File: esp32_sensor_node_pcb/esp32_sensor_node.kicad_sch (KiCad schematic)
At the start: 21 parts, among them J1 Conn_02x10_Top_Bottom, Q1 2N7002K, SW1 SW_DIP_x01, SW2 SW_DIP_x01, U1 HT7833, U2 ESP32-WROOM-E, U3 MAX3483AEASA+

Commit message: Updated schematic
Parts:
- added C6: 22uF, Capacitor_SMD:C_0603_1608Metric, symbol Device:C_Small
- R2: value 500R -> 1.91K
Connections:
- net GND: now also C6.2
- net 3V3 renamed +3.3V
- net +3.3V: now also JST_XH_SOIL5V1.1 (Pin_1), U3.8 (VCC), C6.1
- net 5V renamed +5V
- net +5V: no longer JST_XH_SOIL5V1.1 (Pin_1), U3.8 (VCC)

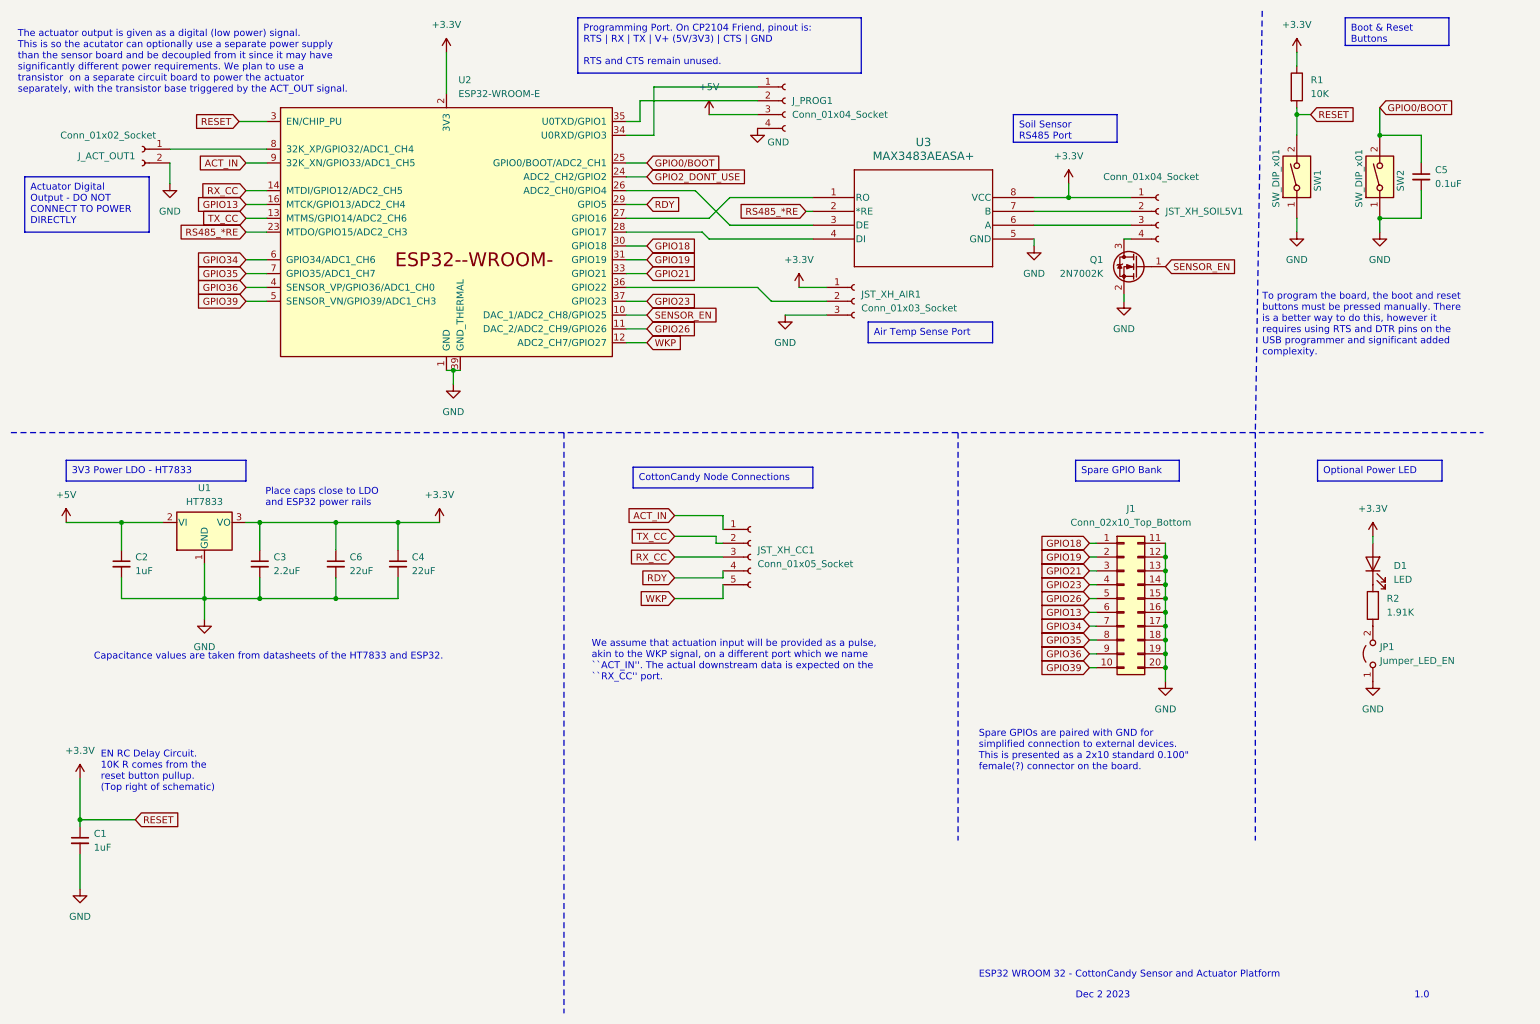
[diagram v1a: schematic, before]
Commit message: Added big 0805 22u capacitor, fixed reset capacitor, add capacitor for max ic decoupling
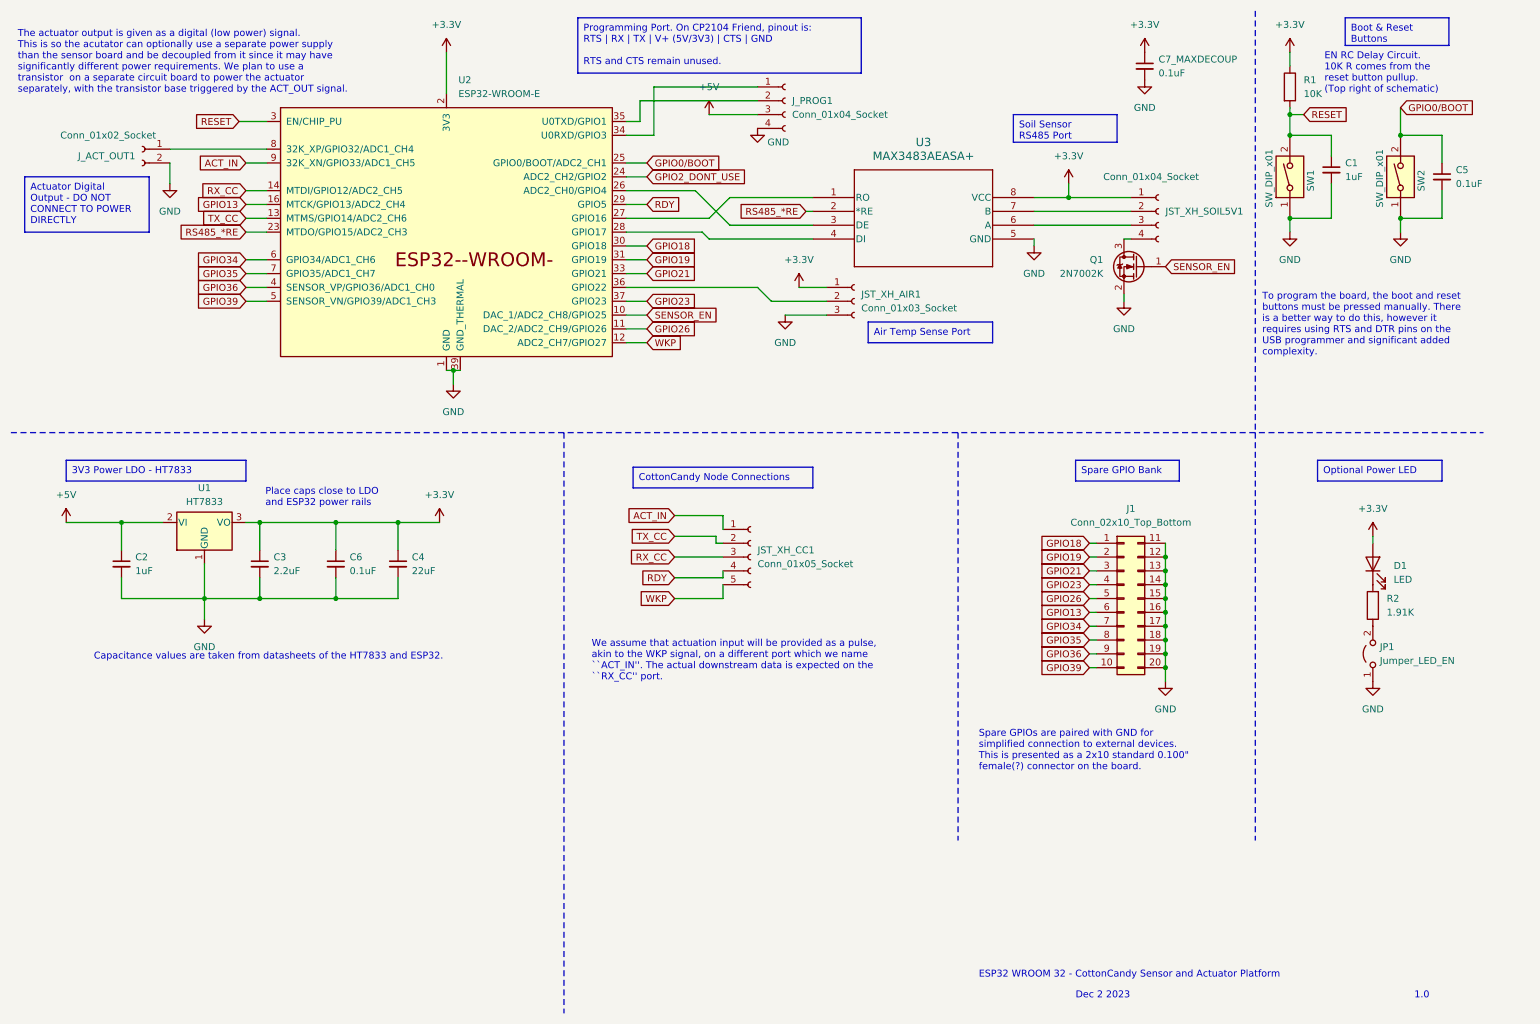
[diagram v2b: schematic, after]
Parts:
- added C7_MAXDECOUP: 0.1uF, Capacitor_SMD:C_0603_1608Metric, symbol Device:C_Small
- C4: footprint Capacitor_SMD:C_0603_1608Metric -> Capacitor_SMD:C_0805_2012Metric
- C6: value 22uF -> 0.1uF
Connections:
- net +3.3V: now also C7_MAXDECOUP.1; no longer C1.1, R1.2, SW1.2, U2.3 (EN/CHIP_PU)
- net GND: now also C7_MAXDECOUP.2
- new net RESET: C1.1, R1.2, SW1.2, U2.3 (EN/CHIP_PU)
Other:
- moved on the sheet: C5, R1, SW1, SW2

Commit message: Add mounting holes
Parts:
- added H1, H2, H3, H4: MountingHole_Pad, MountingHole:MountingHole_3.2mm_M3, symbol Mechanical:MountingHole_Pad
- renumbered C2 to C1, C3 to C2, C6 to C3, C1 to C5, C5 to C6, C7_MAXDECOUP to C7_MAXDECOUP1

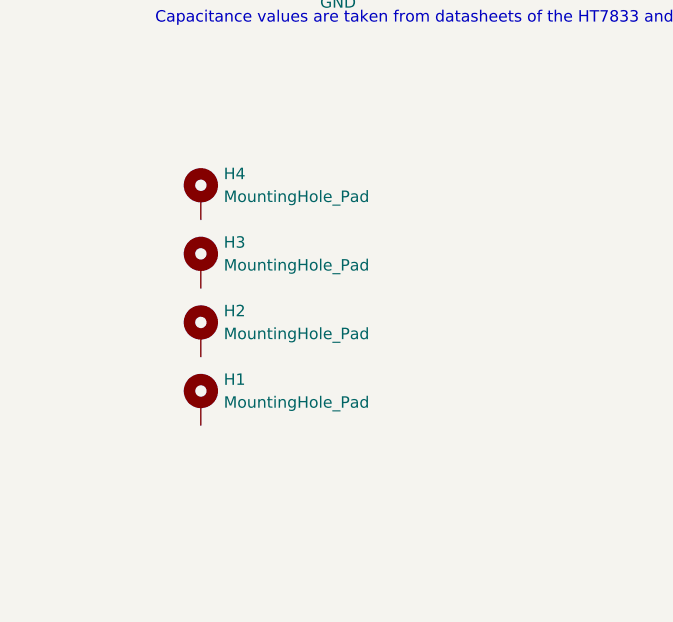
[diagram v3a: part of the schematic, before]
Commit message: Setup initial board layout
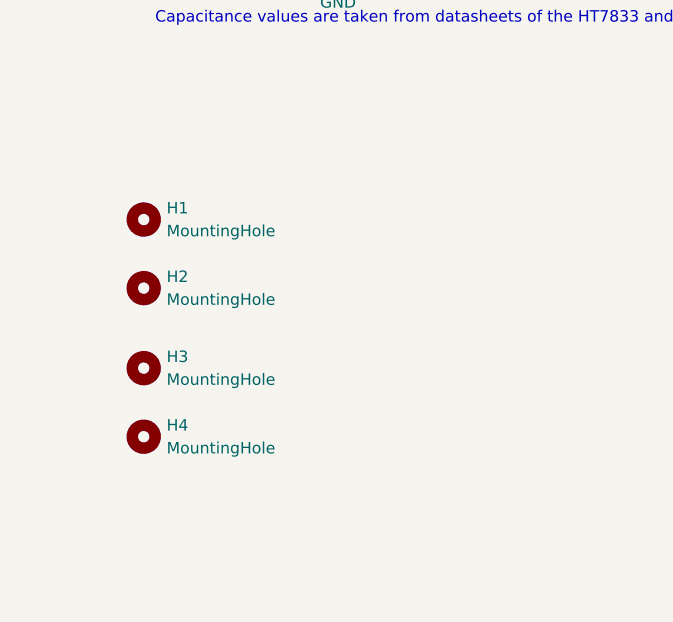
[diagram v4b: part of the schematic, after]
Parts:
- removed H1, H2, H3, H4: MountingHole_Pad, MountingHole:MountingHole_3.2mm_M3, symbol Mechanical:MountingHole_Pad
- added H1, H2, H3, H4: MountingHole, MountingHole:MountingHole_3.2mm_M3, symbol Mechanical:MountingHole
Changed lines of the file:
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@@
-    )
-  )
-  (symbol (lib_id "Mechanical:MountingHole_Pad") (at 33.02 173.99 0) (unit 1)
-    (in_bom yes) (on_board yes) (dnp no) (fields_autoplaced)
-    (property "Reference" "H1" (at 35.56 171.45 0)
-      (effects (font (size 1.27 1.27)) (justify left))
-    )
-    (property "Value" "MountingHole_Pad" (at 35.56 173.99 0)
-      (effects (font (size 1.27 1.27)) (justify left))
-    )
-    (property "Footprint" "MountingHole:MountingHole_3.2mm_M3" (at 33.02 173.99 0)
-      (effects (font (size 1.27 1.27)) hide)
-    )
-    (property "Datasheet" "~" (at 33.02 173.99 0)
-      (effects (font (size 1.27 1.27)) hide)
-    )
-    (pin "1")
-    (instances
-      (project "esp32_sensor_node"
-        (path "/f305b47d-1a34-49f4-94a4-22a58fb9ed31"
-          (reference "H1") (unit 1)
-        )
-      )
     )
   )
@@
     )
   )
-  (symbol (lib_id "Mechanical:MountingHole_Pad") (at 33.02 166.37 0) (unit 1)
-    (in_bom yes) (on_board yes) (dnp no) (fields_autoplaced)
-    (property "Reference" "H2" (at 35.56 163.83 0)
-      (effects (font (size 1.27 1.27)) (justify left))
-    )
-    (property "Value" "MountingHole_Pad" (at 35.56 166.37 0)
-      (effects (font (size 1.27 1.27)) (justify left))
-    )
-    (property "Footprint" "MountingHole:MountingHole_3.2mm_M3" (at 33.02 166.37 0)
-      (effects (font (size 1.27 1.27)) hide)
-    )
-    (property "Datasheet" "~" (at 33.02 166.37 0)
-      (effects (font (size 1.27 1.27)) hide)
-    )
-    (pin "1")
-    (instances
-      (project "esp32_sensor_node"
-        (path "/f305b47d-1a34-49f4-94a4-22a58fb9ed31"
-          (reference "H2") (unit 1)
-        )
-      )
-    )
-  )
   (symbol (lib_id "power:GND") (at 247.65 53.34 0) (unit 1)
     (in_bom yes) (on_board yes) (dnp no) (fields_autoplaced)
@@
         (path "/f305b47d-1a34-49f4-94a4-22a58fb9ed31"
           (reference "JP1") (unit 1)
-        )
-      )
-    )
-  )
-  (symbol (lib_id "Mechanical:MountingHole_Pad") (at 33.02 158.75 0) (unit 1)
-    (in_bom yes) (on_board yes) (dnp no) (fields_autoplaced)
-    (property "Reference" "H3" (at 35.56 156.21 0)
-      (effects (font (size 1.27 1.27)) (justify left))
-    )
-    (property "Value" "MountingHole_Pad" (at 35.56 158.75 0)
-      (effects (font (size 1.27 1.27)) (justify left))
-    )
-    (property "Footprint" "MountingHole:MountingHole_3.2mm_M3" (at 33.02 158.75 0)
-      (effects (font (size 1.27 1.27)) hide)
-    )
-    (property "Datasheet" "~" (at 33.02 158.75 0)
-      (effects (font (size 1.27 1.27)) hide)
-    )
-    (pin "1")
-    (instances
-      (project "esp32_sensor_node"
-        (path "/f305b47d-1a34-49f4-94a4-22a58fb9ed31"
-          (reference "H3") (unit 1)
         )
       )
@@
     )
   )
+  (symbol (lib_id "Mechanical:MountingHole") (at 26.67 170.18 0) (unit 1)
+    (in_bom yes) (on_board yes) (dnp no) (fields_autoplaced)
+    (property "Reference" "H3" (at 29.21 168.91 0)
+      (effects (font (size 1.27 1.27)) (justify left))
+    )
+    (property "Value" "MountingHole" (at 29.21 171.45 0)
+      (effects (font (size 1.27 1.27)) (justify left))
+    )
+    (property "Footprint" "MountingHole:MountingHole_3.2mm_M3" (at 26.67 170.18 0)
+      (effects (font (size 1.27 1.27)) hide)
+    )
+    (property "Datasheet" "~" (at 26.67 170.18 0)
+      (effects (font (size 1.27 1.27)) hide)
+    )
+    (instances
+      (project "esp32_sensor_node"
+        (path "/f305b47d-1a34-49f4-94a4-22a58fb9ed31"
+          (reference "H3") (unit 1)
+        )
+      )
+    )
+  )
   (symbol (lib_id "power:GND") (at 48.26 124.46 0) (unit 1)
     (in_bom yes) (on_board yes) (dnp no) (fields_autoplaced)
@@
     )
   )
+  (symbol (lib_id "Mechanical:MountingHole") (at 26.67 161.29 0) (unit 1)
+    (in_bom yes) (on_board yes) (dnp no) (fields_autoplaced)
+    (property "Reference" "H2" (at 29.21 160.02 0)
+      (effects (font (size 1.27 1.27)) (justify left))
+    )
+    (property "Value" "MountingHole" (at 29.21 162.56 0)
+      (effects (font (size 1.27 1.27)) (justify left))
+    )
+    (property "Footprint" "MountingHole:MountingHole_3.2mm_M3" (at 26.67 161.29 0)
+      (effects (font (size 1.27 1.27)) hide)
+    )
+    (property "Datasheet" "~" (at 26.67 161.29 0)
+      (effects (font (size 1.27 1.27)) hide)
+    )
+    (instances
+      (project "esp32_sensor_node"
+        (path "/f305b47d-1a34-49f4-94a4-22a58fb9ed31"
+          (reference "H2") (unit 1)
+        )
+      )
+    )
+  )
+  (symbol (lib_id "Mechanical:MountingHole") (at 26.67 153.67 0) (unit 1)
+    (in_bom yes) (on_board yes) (dnp no) (fields_autoplaced)
+    (property "Reference" "H1" (at 29.21 152.4 0)
+      (effects (font (size 1.27 1.27)) (justify left))
+    )
+    (property "Value" "MountingHole" (at 29.21 154.94 0)
+      (effects (font (size 1.27 1.27)) (justify left))
+    )
+    (property "Footprint" "MountingHole:MountingHole_3.2mm_M3" (at 26.67 153.67 0)
+      (effects (font (size 1.27 1.27)) hide)
+    )
+    (property "Datasheet" "~" (at 26.67 153.67 0)
+      (effects (font (size 1.27 1.27)) hide)
+    )
+    (instances
+      (project "esp32_sensor_node"
+        (path "/f305b47d-1a34-49f4-94a4-22a58fb9ed31"
+          (reference "H1") (unit 1)
+        )
+      )
+    )
+  )
   (symbol (lib_id "power:GND") (at 220.98 25.4 0) (unit 1)
     (in_bom yes) (on_board yes) (dnp no) (fields_autoplaced)
@@
         (path "/f305b47d-1a34-49f4-94a4-22a58fb9ed31"
           (reference "#PWR015") (unit 1)
+        )
+      )
+    )
+  )
+  (symbol (lib_id "Mechanical:MountingHole") (at 26.67 177.8 0) (unit 1)
+    (in_bom yes) (on_board yes) (dnp no) (fields_autoplaced)
+    (property "Reference" "H4" (at 29.21 176.53 0)
+      (effects (font (size 1.27 1.27)) (justify left))
+    )
+    (property "Value" "MountingHole" (at 29.21 179.07 0)
+      (effects (font (size 1.27 1.27)) (justify left))
+    )
+    (property "Footprint" "MountingHole:MountingHole_3.2mm_M3" (at 26.67 177.8 0)
+      (effects (font (size 1.27 1.27)) hide)
+    )
+    (property "Datasheet" "~" (at 26.67 177.8 0)
+      (effects (font (size 1.27 1.27)) hide)
+    )
+    (instances
+      (project "esp32_sensor_node"
+        (path "/f305b47d-1a34-49f4-94a4-22a58fb9ed31"
+          (reference "H4") (unit 1)
         )
       )
@@
         )
       )
-    )
-  )
-  (symbol (lib_id "Mechanical:MountingHole_Pad") (at 33.02 151.13 0) (unit 1)
-    (in_bom yes) (on_board yes) (dnp no) (fields_autoplaced)
-    (property "Reference" "H4" (at 35.56 148.59 0)
-      (effects (font (size 1.27 1.27)) (justify left))
-    )
-    (property "Value" "MountingHole_Pad" (at 35.56 151.13 0)
-      (effects (font (size 1.27 1.27)) (justify left))
-    )
-    (property "Footprint" "MountingHole:MountingHole_3.2mm_M3" (at 33.02 151.13 0)
-      (effects (font (size 1.27 1.27)) hide)
-    )
-    (property "Datasheet" "~" (at 33.02 151.13 0)
-      (effects (font (size 1.27 1.27)) hide)
-    )
-    (pin "1")
-    (instances
-      (project "esp32_sensor_node"
-        (path "/f305b47d-1a34-49f4-94a4-22a58fb9ed31"
-          (reference "H4") (unit 1)
-        )
-      )

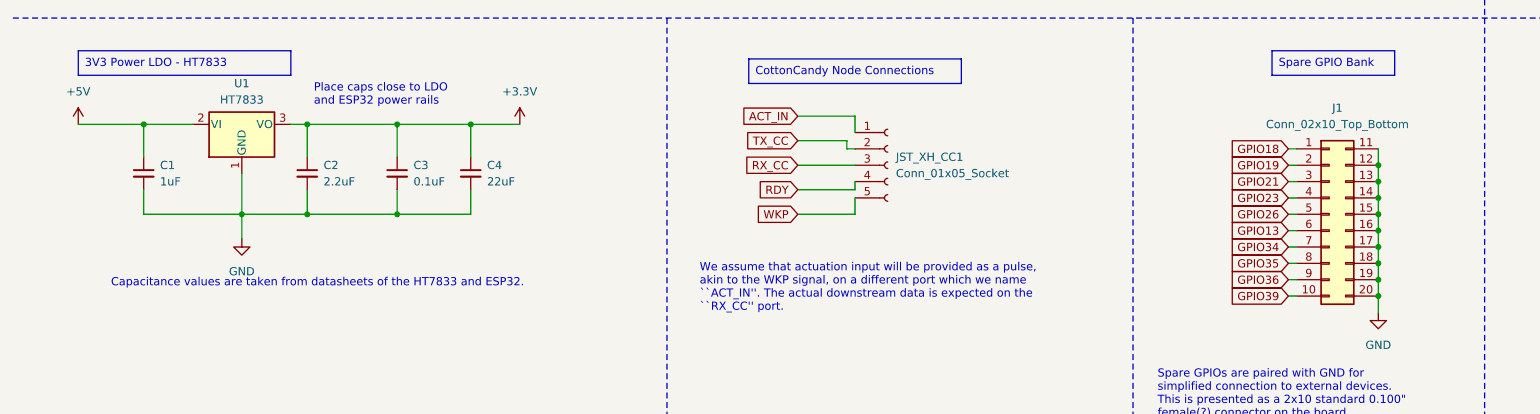
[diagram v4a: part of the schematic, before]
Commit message: Complete first draft routing
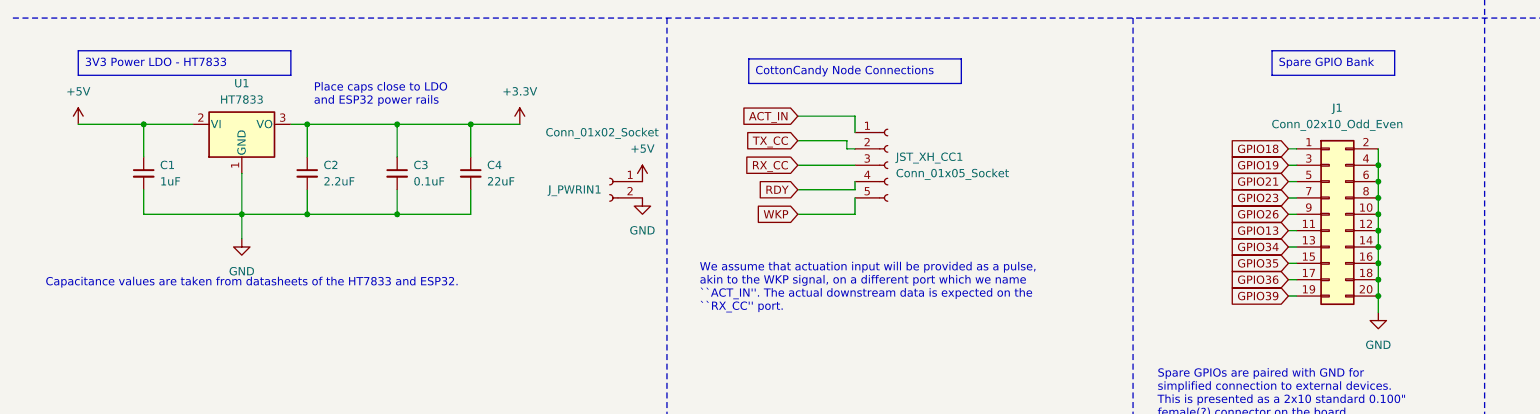
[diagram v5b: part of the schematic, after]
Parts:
- removed J1: Conn_02x10_Top_Bottom, Connector_PinSocket_2.54mm:PinSocket_2x10_P2.54mm_Vertical, symbol Connector_Generic:Conn_02x10_Top_Bottom
- added J1: Conn_02x10_Odd_Even, Connector_PinSocket_2.54mm:PinSocket_2x10_P2.54mm_Vertical, symbol Connector_Generic:Conn_02x10_Odd_Even
- added J_PWRIN1: Conn_01x02_Socket, Connector_JST:JST_XH_B2B-XH-A_1x02_P2.50mm_Vertical, symbol Connector:Conn_01x02_Socket
- JST_XH_AIR1: footprint Connector_JST:JST_XH_B3B-XH-AM_1x03_P2.50mm_Vertical -> Connector_JST:JST_XH_B3B-XH-A_1x03_P2.50mm_Vertical
- JST_XH_CC1: footprint Connector_JST:JST_XH_B5B-XH-AM_1x05_P2.50mm_Vertical -> Connector_JST:JST_XH_B5B-XH-A_1x05_P2.50mm_Vertical
- JST_XH_SOIL5V1, J_PROG1: footprint Connector_JST:JST_XH_B4B-XH-AM_1x04_P2.50mm_Vertical -> Connector_JST:JST_XH_B4B-XH-A_1x04_P2.50mm_Vertical
- J_ACT_OUT1: footprint Connector_JST:JST_XH_B2B-XH-AM_1x02_P2.50mm_Vertical -> Connector_JST:JST_XH_B2B-XH-A_1x02_P2.50mm_Vertical
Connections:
- net +5V: now also J_PWRIN1.1 (Pin_1)
- net GND: now also J1.10 (Pin_10), J1.12 (Pin_12), J1.14 (Pin_14), J1.16 (Pin_16), J1.18 (Pin_18), J1.2 (Pin_2), J1.20 (Pin_20), J1.4 (Pin_4), J1.6 (Pin_6), J1.8 (Pin_8), J_PWRIN1.2 (Pin_2)
- net GPIO13: now also J1.11 (Pin_11)
- net GPIO18: now also J1.1 (Pin_1)
- net GPIO19: now also J1.3 (Pin_3)
- net GPIO21: now also J1.5 (Pin_5)
- net GPIO23: now also J1.7 (Pin_7)
- net GPIO26: now also J1.9 (Pin_9)
- net GPIO34: now also J1.13 (Pin_13)
- net GPIO35: now also J1.15 (Pin_15)
- net GPIO36: now also J1.17 (Pin_17)
- net GPIO39: now also J1.19 (Pin_19)
